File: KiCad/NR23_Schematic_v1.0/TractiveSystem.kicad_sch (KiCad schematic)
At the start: 32 parts, among them M1 Zero_7R_Motor

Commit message: start of class 18APR23
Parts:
- removed J?: Dash 12 power connection, symbol Connector_Generic:Conn_01x02
- gave numbers to parts that had none: 1
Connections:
- net Battery CAN High is gone; now on net CAN_High_fromBattery: BTmain.P5 (CAN_H)
- net Battery CAN Low is gone; now on net CAN_Low_fromBattery: BTmain.S4 (CAN_L)
- net Cont1 Supply (+): now also U?.4 (Cont1_Supply_(+))
- net Line Contactor (Cont1): now also U?.3 (Line_Contactor_(Cont1))
- net EnA: now reaches J?.1 (Pin_1), U?.21 (encoder_A)
- net EnB: now reaches J?.2 (Pin_2), U?.35 (encoder_B)
- net 0_V: now reaches J?.3 (Pin_3), U?.15 (0_V)
- net 10V: now reaches J?.4 (Pin_4), U?.26 (+10V)
- net B-: now reaches BTmain.(-), J?.5 (Pin_5), U?. (M3)
- net R_th: now reaches J?.6 (Pin_6), U?.33 (Thermistor)
- net Key Switch In: now reaches K?.4, U?.1 (Key_Switch_In), U?.6 (Key_Switch_In)
- net at BTmain.(+): now also HVSS.2 (B); no longer HVSS.1 (A)
- net Batt CAN PWR: now reaches BTmain.P2 (CAN_5V)
- net Batt CAN GND: now reaches BTmain.S2 (CAN_GND)
- net at K?.3: now also HVSS.1 (A); no longer HVSS.2 (B)
- no-connect marks 5 -> 7
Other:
- note added: "12V Battery Box"
- note added: "Crane said not to use the 12V from the battery.Use Alt 12V or DC-DC converter"
- note added: "Harness 5: Dash to Battery Box"
- note added: "High Voltage Switch Box"
- note removed: "?Where is the Key Switch Relay physically located?"
- note removed: "?Where is the Line Contactor Relay physically located?"
- note removed: "Aux 12V battery | Main battery"
- note removed: "Harness 5: Dash to Keyswitch"
- moved on the sheet: BTaux, F?, HVSS, J?, M1, SW?

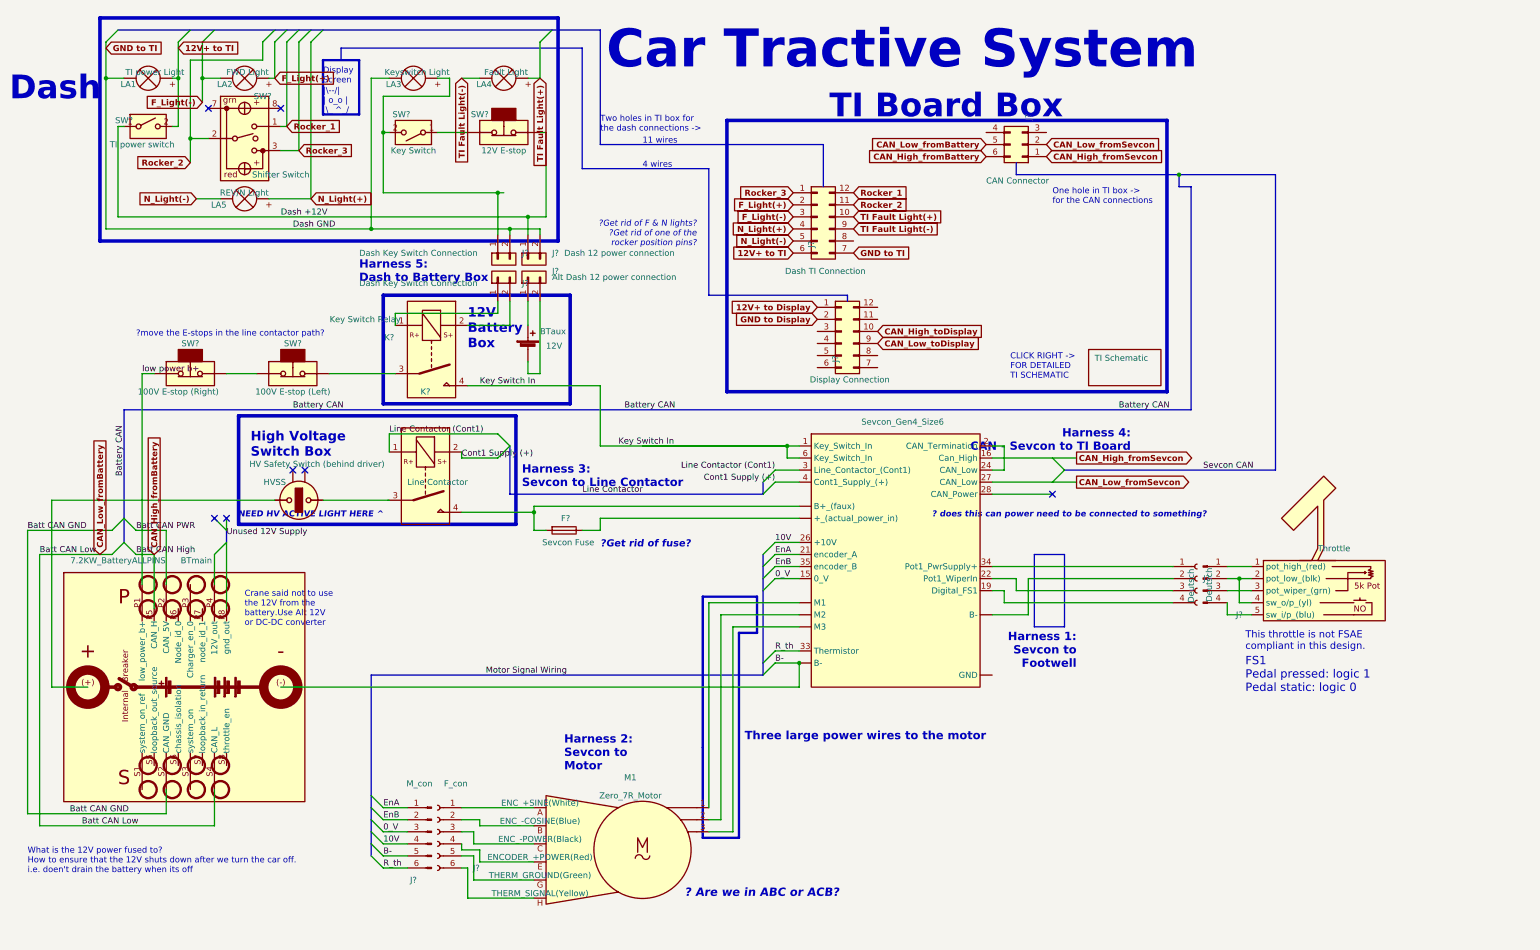
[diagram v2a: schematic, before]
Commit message: endof day 26APR23
changed the wires going into the ti board box in order to match what is actually on the car
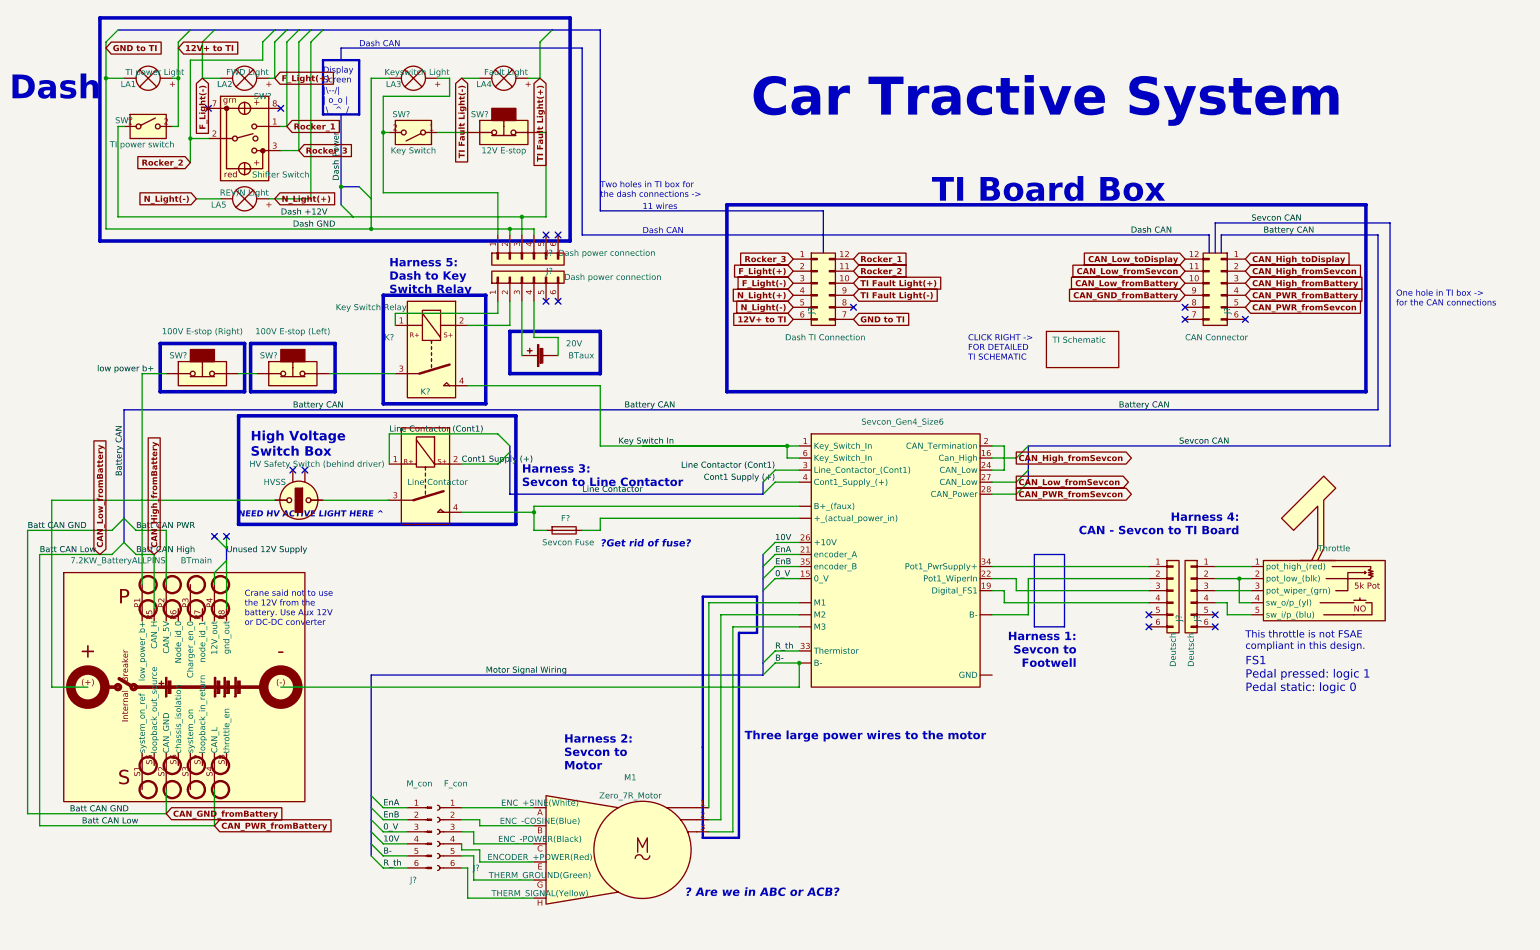
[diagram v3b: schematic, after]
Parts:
- removed J?: Deutsch, symbol Connector:Conn_01x04_Male
- removed J? (x2): Dash Key Switch Connection, symbol Connector_Generic:Conn_01x02
- removed J?: Deutsch, symbol Connector:Conn_01x04_Female
- removed J?: Display Connection, symbol Connector_Generic:Conn_02x06_Counter_Clockwise
- added J? (x2): Deutsch, symbol Connector_Generic:Conn_01x06
- BTaux: value 12V -> 20V
- J?: symbol Connector_Generic:Conn_02x03_Counter_Clockwise -> Connector_Generic:Conn_02x06_Counter_Clockwise
- J?: value Alt Dash 12 power connection -> Dash power connection; symbol Connector_Generic:Conn_01x02 -> Connector_Generic:Conn_01x06
- J?: value Dash 12 power connection -> Dash power connection; symbol Connector_Generic:Conn_01x02 -> Connector_Generic:Conn_01x06
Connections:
- net CAN_High_fromBattery: now also J?.3 (Pin_3); no longer J?.6 (Pin_6)
- net CAN_High_fromSevcon: now also J?.2 (Pin_2); no longer J?.1 (Pin_1)
- net CAN_High_toDisplay: now also J?.1 (Pin_1)
- net CAN_Low_fromBattery: now also J?.10 (Pin_10), J?.4 (Pin_4); no longer J?.5 (Pin_5)
- net CAN_Low_fromSevcon: now also J?.11 (Pin_11); no longer J?.2 (Pin_2)
- net CAN_Low_toDisplay: now also J?.12 (Pin_12)
- net Dash +12V: now also J?.3 (Pin_3); no longer J?.1 (Pin_1)
- net GND to TI: now also J?.4 (Pin_4)
- net at U?.1 (pot_high_(red)): now also J?.1 (Pin_1)
- net at U?.2 (pot_low_(blk)), U?.4 (sw_o/p_(yl)): now also J?.2 (Pin_2)
- net at U?.3 (pot_wiper_(grn)): now also J?.3 (Pin_3)
- net at U?.5 (sw_i/p_(blu)): now also J?.4 (Pin_4)
- net at LA3.2 (+), SW?.2 (B): now also J?.1 (Pin_1)
- net at BTaux.1 (+): now also J?.3 (Pin_3); no longer J?.1 (Pin_1)
- net at BTaux.2 (-): now also J?.4 (Pin_4); no longer J?.2 (Pin_2)
- net at U?.19 (Digital_FS1): now also J?.4 (Pin_4)
- net at U?.22 (Pot1_WiperIn): now also J?.3 (Pin_3)
- net CAN_PWR_fromSevcon: now reaches U?.28 (CAN_Power)
- net CAN_PWR_fromSevcon: now also J?.5 (Pin_5)
- net at U?.34 (Pot1_PwrSupply+): now also J?.1 (Pin_1)
- net at K?.1: now also J?.1 (Pin_1)
- net at K?.2: now also J?.2 (Pin_2)
- net Batt CAN GND renamed CAN_GND_fromBattery
- net CAN_GND_fromBattery: now also J?.9 (Pin_9)
- new net: J?.2 (Pin_2), U?. (M3)
- no-connect marks 7 -> 18
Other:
- note added: "Crane said not to use the 12V from the battery. Use Aux 12V or DC-DC converter"
- note added: "Dash CAN"
- note added: "Harness 5: Dash to Key Switch Relay"
- note removed: "12V Battery Box"
- note removed: "4 wires"
- note removed: "? does this can power need to be connected to something?"
- note removed: "?Get rid of F & N lights? ?Get rid of one of the rocker position pins?"
- note removed: "?move the E-stops in the line contactor path?"
- note removed: "Crane said not to use the 12V from the battery.Use Alt 12V or DC-DC converter"
- note removed: "Harness 5: Dash to Battery Box"
- note removed: "What is the 12V power fused to? How to ensure that the 12V shuts down after we turn the car off. i.e. doen't drain the battery when its off"
- moved on the sheet: BTaux, J?, SW?

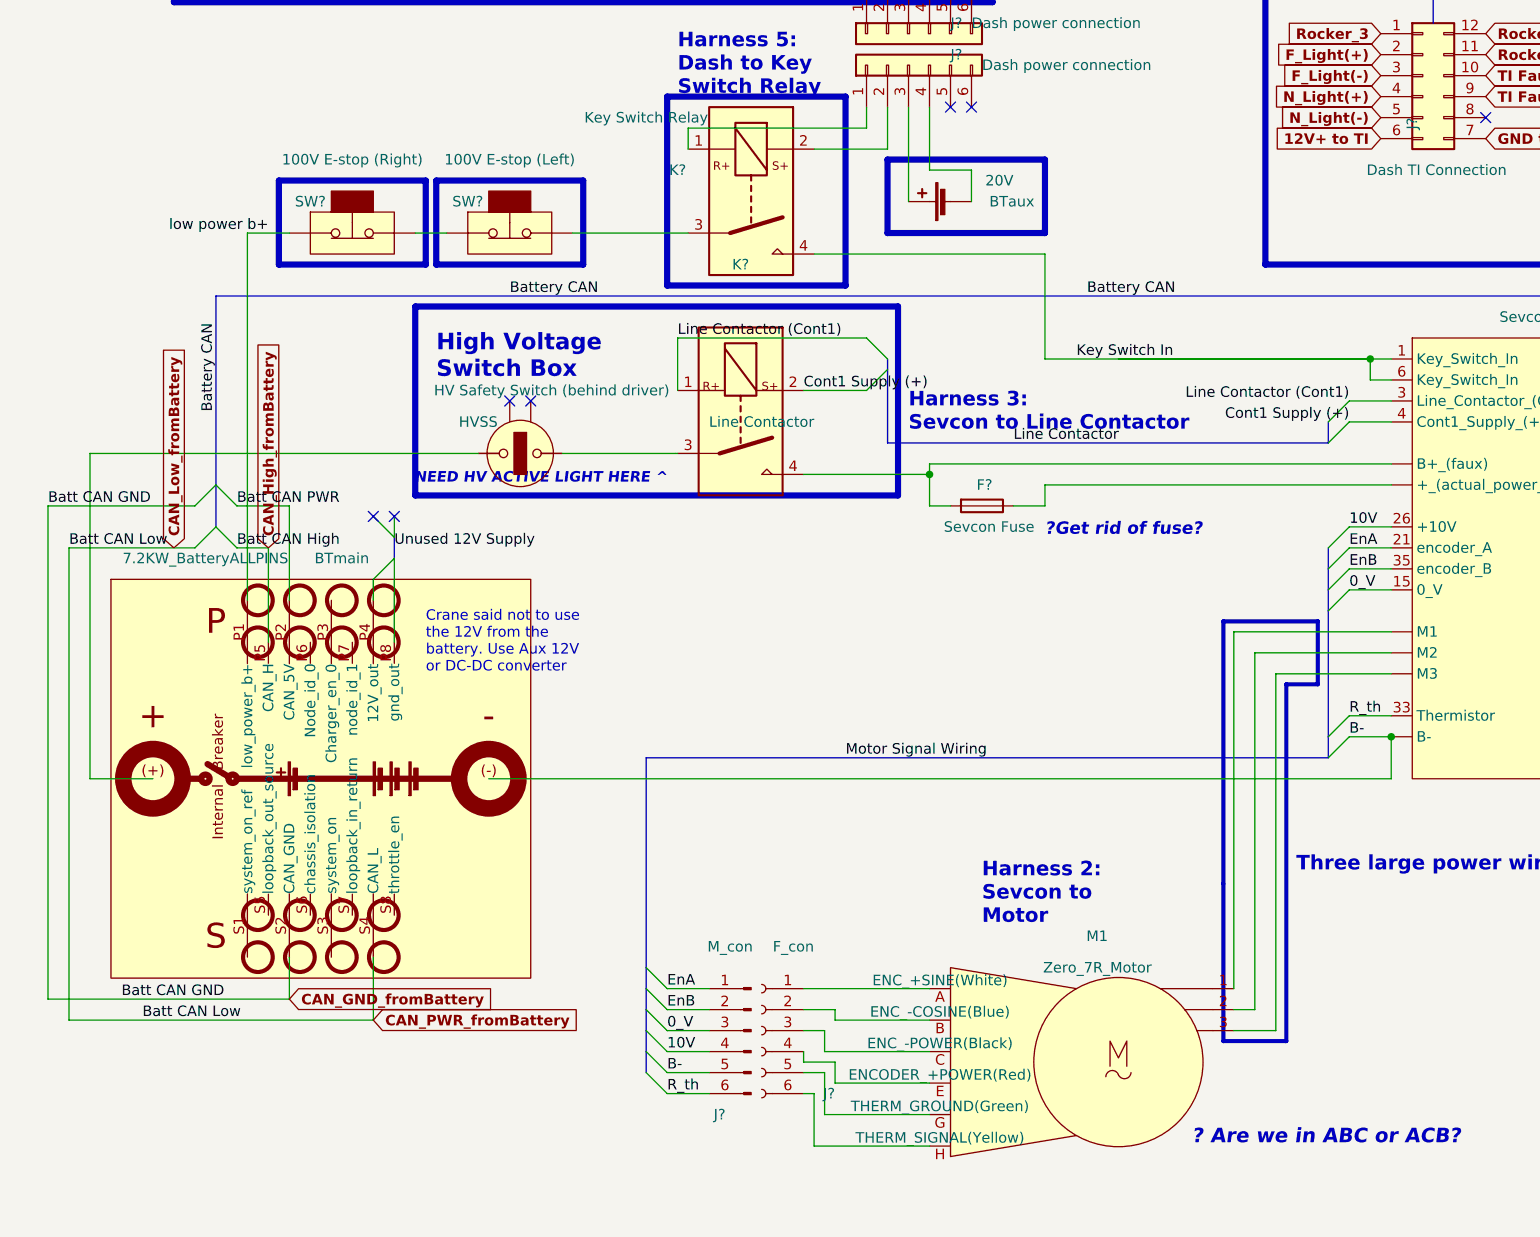
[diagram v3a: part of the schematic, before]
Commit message: end of class on 01APR23 - battery stuff
Added new battery connections and reprinted battery schematic
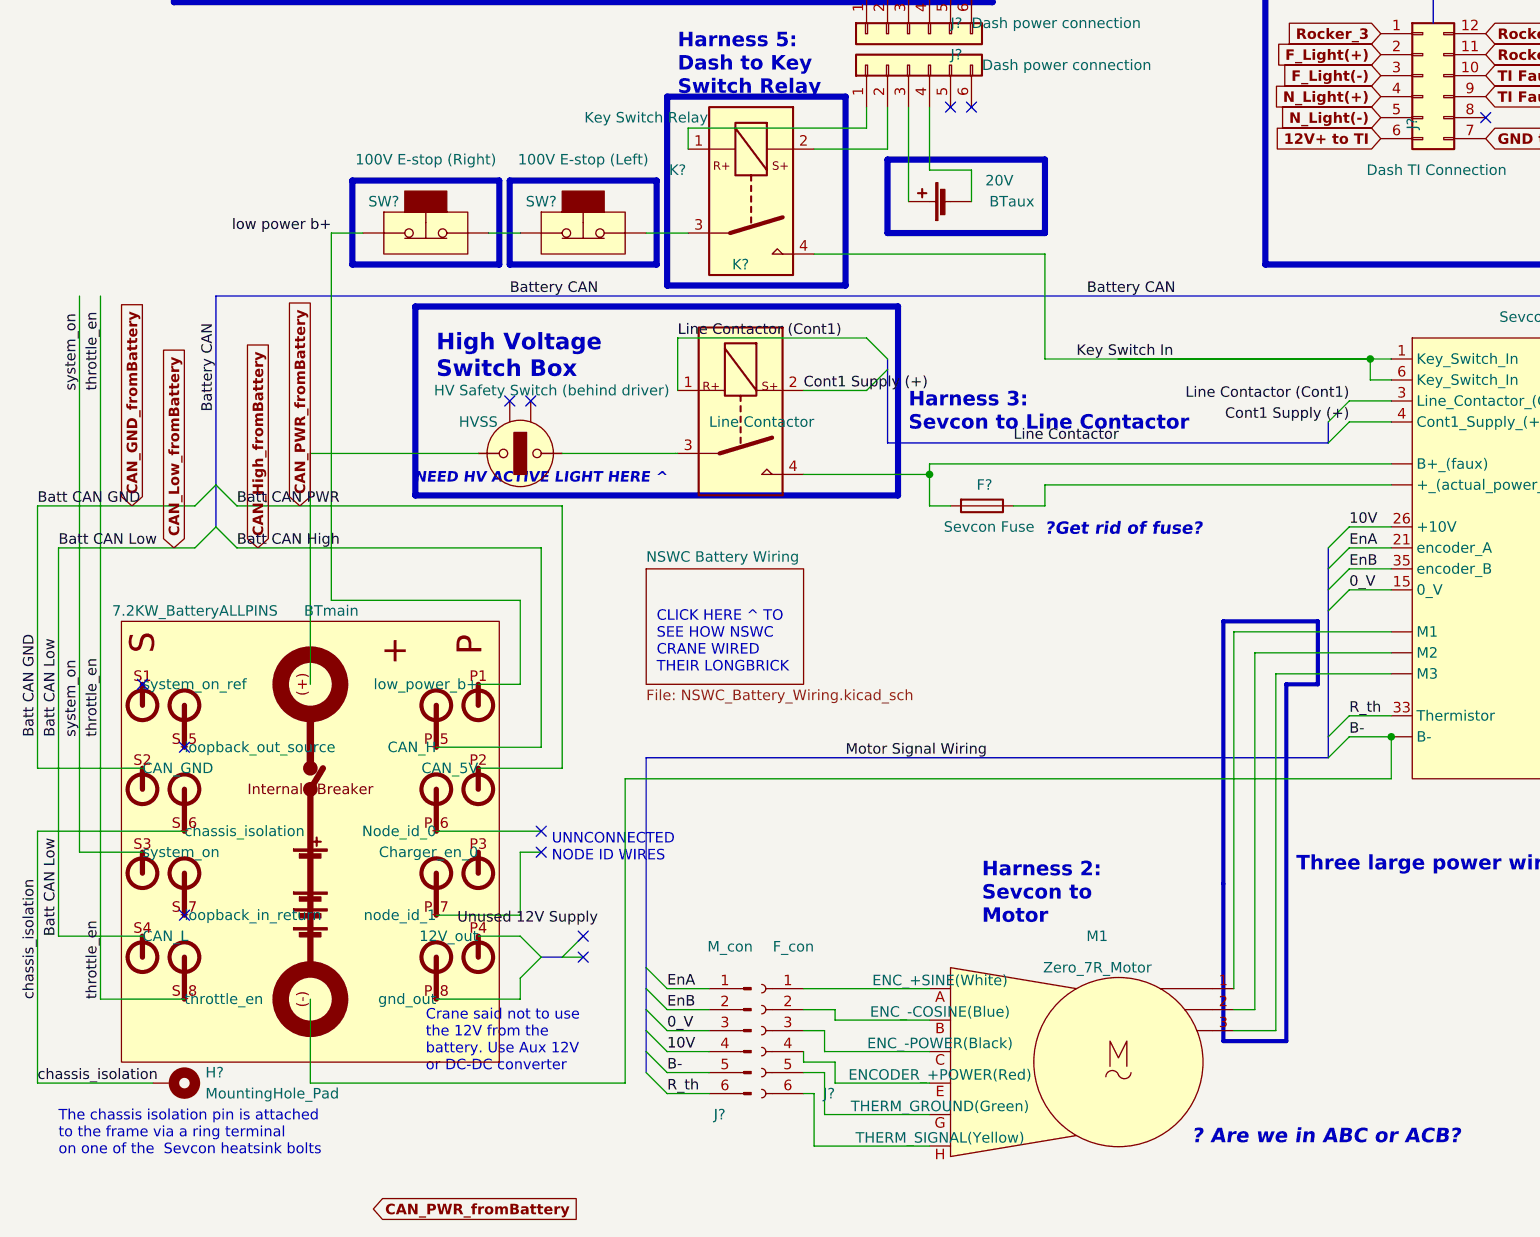
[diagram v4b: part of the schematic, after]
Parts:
- added H?: MountingHole_Pad, symbol Mechanical:MountingHole_Pad
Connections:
- net CAN_High_fromBattery: now also BTmain.P_5 (CAN_H); no longer BTmain.P5 (CAN_H)
- net CAN_Low_fromBattery: no longer J?.4 (Pin_4)
- net system_on: now reaches BTmain.S3 (system_on)
- net Batt CAN PWR renamed CAN_PWR_fromBattery
- net CAN_PWR_fromBattery: now also J?.4 (Pin_4)
- new net chassis_isolation: BTmain.S_6 (chassis_isolation), H?.1
- new net throttle_en: BTmain.S_8 (throttle_en)
- no-connect marks 18 -> 23
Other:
- added sheet NSWC Battery Wiring (NSWC_Battery_Wiring.kicad_sch)
- note added: "CLICK HERE ^ TO SEE HOW NSWC CRANE WIRED THEIR LONGBRICK"
- note added: "The chassis isolation pin is attached to the frame via a ring terminal on one of the Sevcon heatsink bolts"
- note added: "UNNCONNECTED NODE ID WIRES"
- moved on the sheet: SW?

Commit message: end of day 02APR23
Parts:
- gave numbers to parts that had none: 20
- renumbered BTaux to BTaux1, BTmain to BTmain1, HVSS to HVSS1
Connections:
- net system_on renamed system_on_fromBattery
- net throttle_en renamed throttle_en_fromBattery
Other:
- note added: "Fuse is not installed but could be installed in this location"
- note added: "Unused 12V Supply"
- note removed: "?Get rid of fuse?"
- moved on the sheet: BTaux1, HVSS1, K1
